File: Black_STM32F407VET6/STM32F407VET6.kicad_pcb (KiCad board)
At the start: 2 copper layers, 97 parts, among them J1 T0, J10 - HotBed +, J11 Heater0, J12 X-, J13 Y-, J14 Z-, J15 Z+, J16 USB_B, J17 X_logic, J18 Y_logic, J19 Z_logic, J2 T1, J20 E0_logic, J22 Left, J23 EXP2, J24 LCD2004, J25 Bottom, J26 Right, J27 Z_motor, J28 LIGHTS, J29 Z, J3 TB, J30 Z, J33 X_motor, J34 Y_motor, J36 E0_motor, J38 X, J39 Y, J4 TC, J41 E0, J43 Heater1, J44 COM, J47 I2C, J48 SPI, J49 SPI, J5 + VIN -, J50 SDIO, J51 Servo, J52 Servo, J53 PowerSelect, J54 Power, J55 PD11, J56 Power, J6 Fan3, J7 Fan2, J8 Fan1, J9 Fan0, Q1 BCX70, Q10 BCX70, Q11 BCX70, Q12 IRLR8726PBF, Q13 IRLR8726PBF, Q14 IRLR8726PBF, Q2 BCX70, Q3 BCX70, Q4 IRLML0030TRPBF, Q5 BCX70, Q6 IRLML0030TRPBF, Q7 IRLML0030TRPBF, Q8 IRLML0030TRPBF, Q9 BCX70, SW1 Boot0, U5 AT24CS01-SSHM

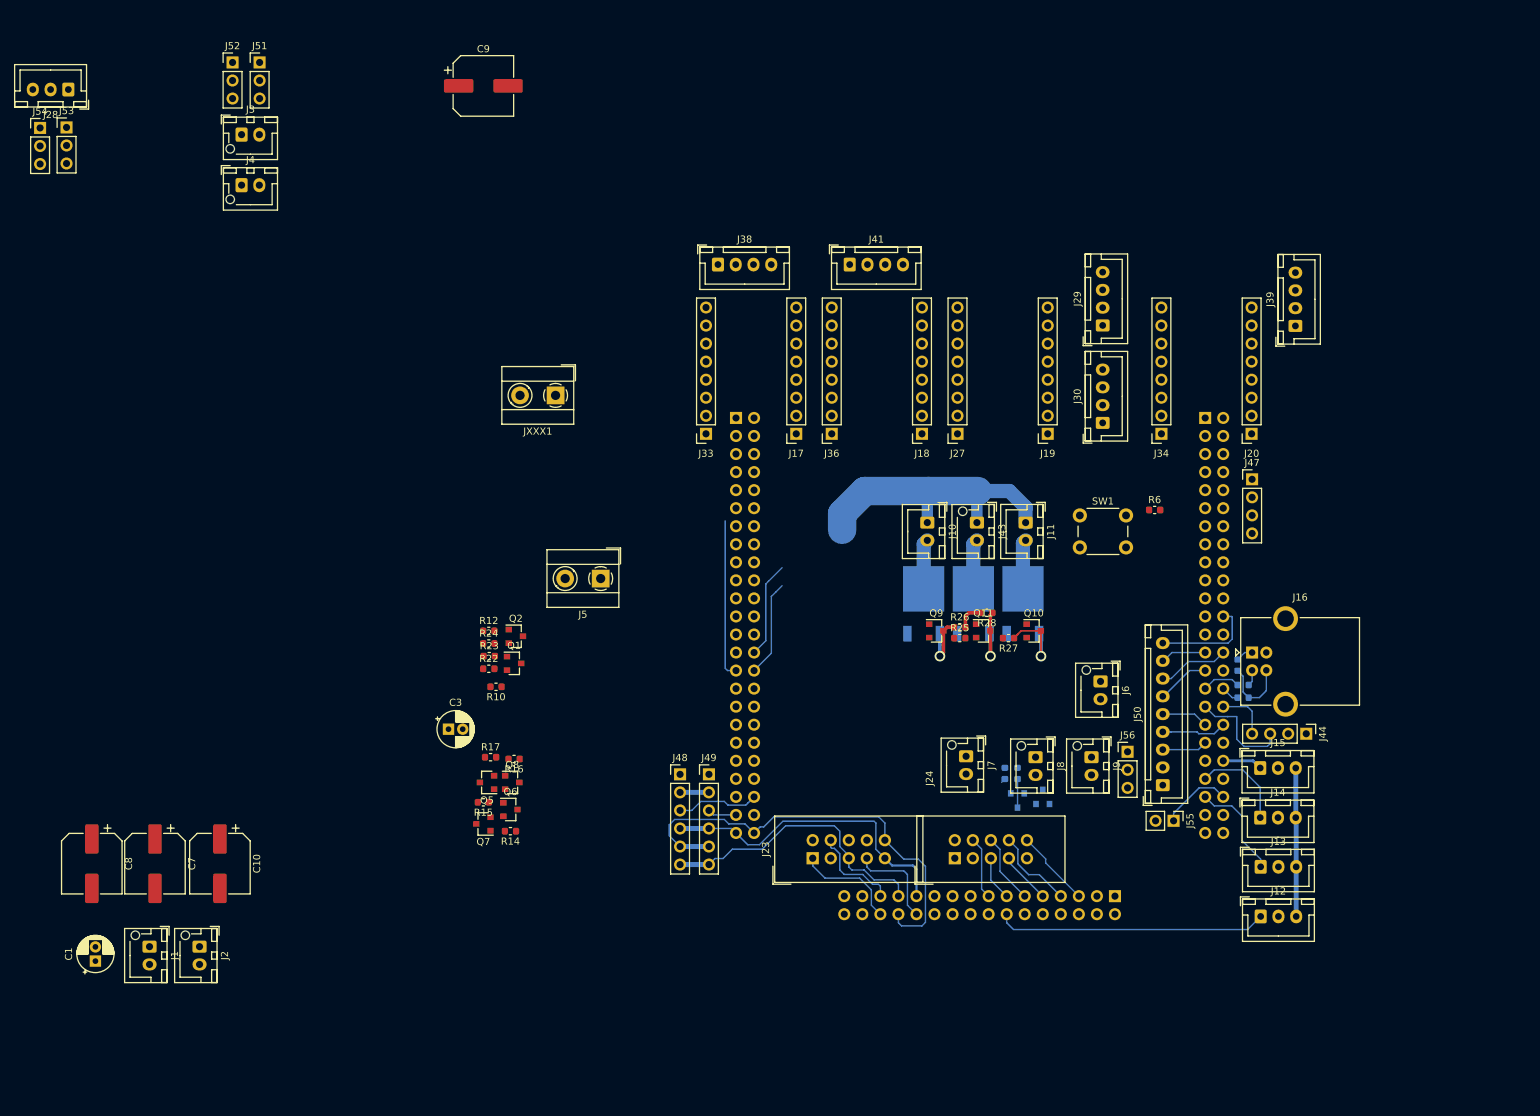
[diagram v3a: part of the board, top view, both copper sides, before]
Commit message: Rework of the PCB, made footprint for the motor drivers.
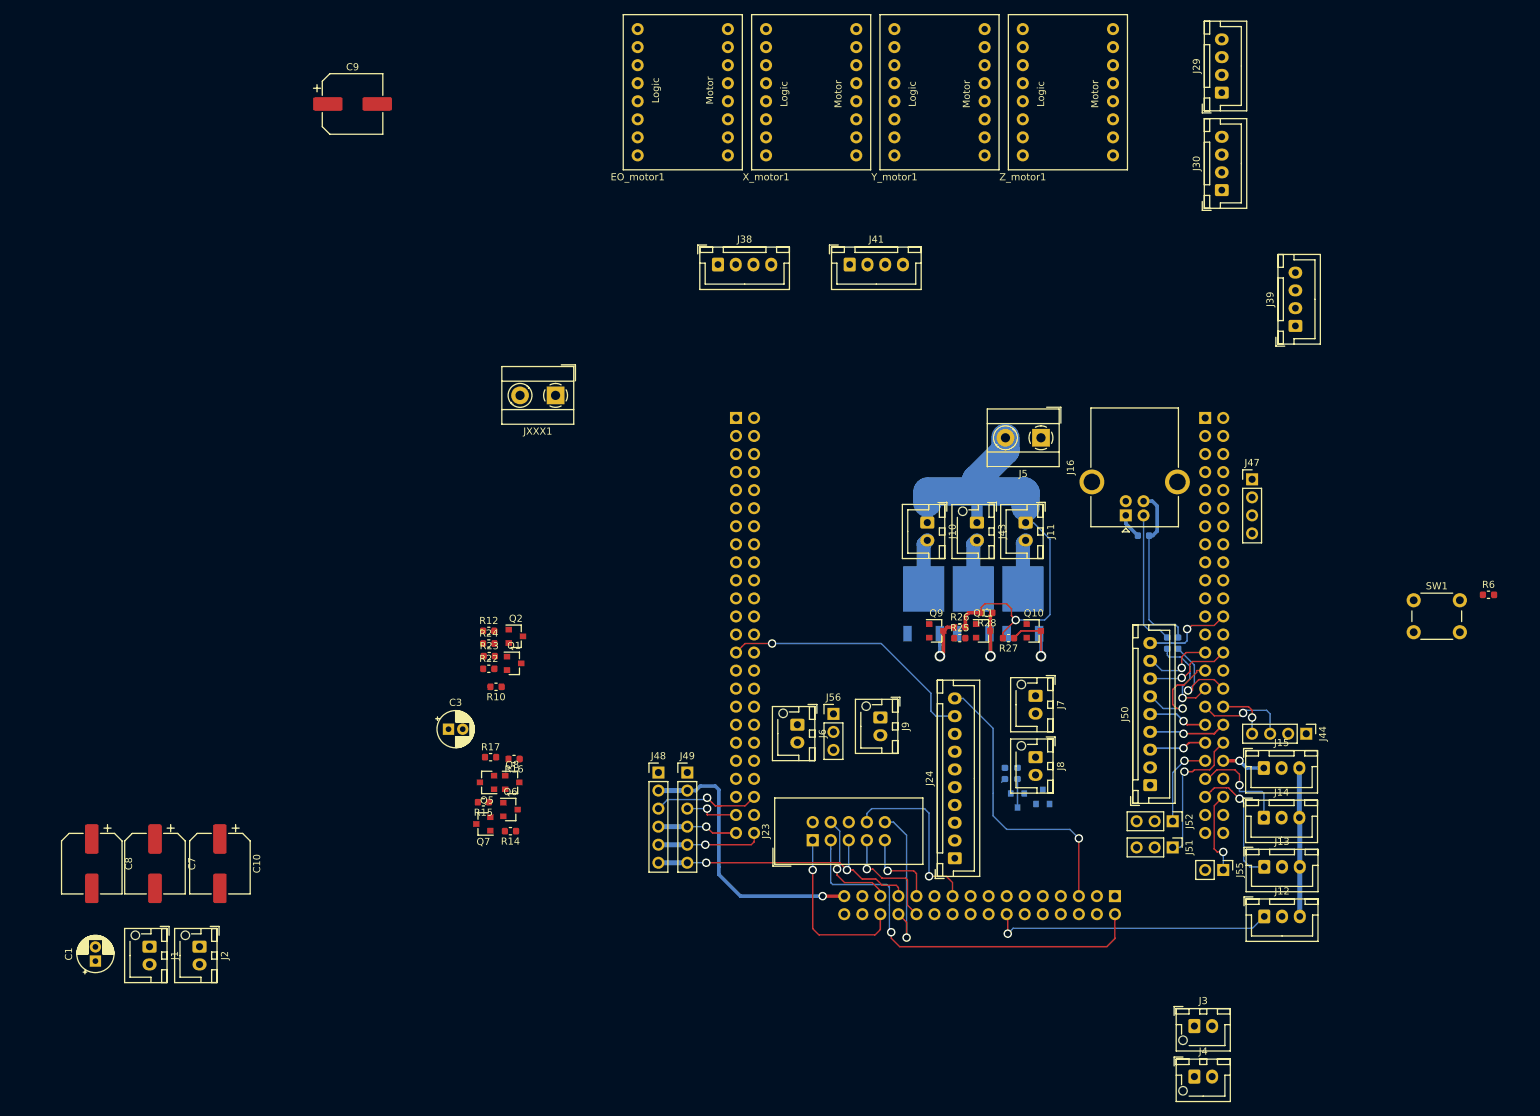
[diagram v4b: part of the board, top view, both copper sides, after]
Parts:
- removed J17: X_logic, Connector_PinSocket_2.54mm:PinSocket_1x08_P2.54mm_Vertical
- removed J18: Y_logic, Connector_PinSocket_2.54mm:PinSocket_1x08_P2.54mm_Vertical
- removed J19: Z_logic, Connector_PinSocket_2.54mm:PinSocket_1x08_P2.54mm_Vertical
- removed J20: E0_logic, Connector_PinSocket_2.54mm:PinSocket_1x08_P2.54mm_Vertical
- removed J27: Z_motor, Connector_PinSocket_2.54mm:PinSocket_1x08_P2.54mm_Vertical
- removed J28: LIGHTS, Connector_JST:JST_XH_B3B-XH-A_1x03_P2.50mm_Vertical
- removed J33: X_motor, Connector_PinSocket_2.54mm:PinSocket_1x08_P2.54mm_Vertical
- removed J34: Y_motor, Connector_PinSocket_2.54mm:PinSocket_1x08_P2.54mm_Vertical
- removed J36: E0_motor, Connector_PinSocket_2.54mm:PinSocket_1x08_P2.54mm_Vertical
- removed J53: PowerSelect, Connector_PinHeader_2.54mm:PinHeader_1x03_P2.54mm_Vertical
- removed J54: Power, Connector_PinHeader_2.54mm:PinHeader_1x03_P2.54mm_Vertical
- added EO_motor1: Step_stick, Motor_driver:Motor, F.Cu at (106.0, 48.9)
- added X_motor1: Step_stick, Motor_driver:Motor, F.Cu at (124.1, 48.9)
- added Y_motor1: Step_stick, Motor_driver:Motor, F.Cu at (142.2, 48.9)
- added Z_motor1: Step_stick, Motor_driver:Motor, F.Cu at (160.3, 48.9)
- C10, C7, C8, C9: value 100uF 35V -> 100uF
- J24: footprint Connector_IDC:IDC-Header_2x05_P2.54mm_Vertical -> Connector_JST:JST_XH_B10B-XH-A_1x10_P2.50mm_Vertical
- moved J3 183.7 mm to (186.4, 169.4)
- moved J4 183.7 mm to (186.4, 176.5)
- moved J52 170.1 mm to (183.4, 140.6), turned to 270 degrees
- moved J51 169.5 mm to (183.4, 144.3), turned to 270 degrees
- moved J5 65.1 mm to (164.8, 86.6)
- moved R6 48.5 mm to (227.8, 108.7)
- moved SW1 48.5 mm to (217.3, 109.5)
- moved J6 43.1 mm to (130.6, 127.0)
- moved J56 41.7 mm to (135.6, 125.5)
- moved J29 36.8 mm to (190.3, 38.0)
- moved J30 36.8 mm to (190.3, 51.7)
- moved J9 30.2 mm to (142.2, 126.0)
- moved J16 26.2 mm to (176.8, 97.5), turned to 90 degrees
- moved R5 22.5 mm to (179.3, 100.4), turned to 180 degrees
- moved C9 18.6 mm to (67.9, 39.6)
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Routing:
- net Reset: track 0.00 -> 57.7 mm, vias 0 -> 1
- net KEYPAD_PIN: track 0.00 -> 37.0 mm, vias 0 -> 1
- net 3V3: track 4.06 -> 39.8 mm, vias 0 -> 1
- net LCD7: track 10.9 -> 41.0 mm, vias 0 -> 1
- net MISO: track 63.5 -> 36.9 mm, vias 0 -> 2
- net 12V: track 45.5 -> 71.1 mm, vias 0 -> 1
- net EN1: track 0.00 -> 25.0 mm, vias 0 -> 1
- net Tmc_MISO: track 22.4 -> 0.00 mm
- net CLK: track 44.3 -> 23.2 mm, vias 0 -> 2
- net PWM2: track 0.00 -> 20.2 mm, vias 0 -> 1
- net Net-(J16-Pad2): track 2.27 -> 19.5 mm
- net Net-(J16-Pad3): track 10.2 -> 25.0 mm
- net Tmc_MOSI: track 13.6 -> 0.00 mm
- net Tmc_SCK: track 13.6 -> 0.00 mm
- net PWM1: track 0.00 -> 12.1 mm, vias 0 -> 1
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
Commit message: Power connectors - Removed left side holes to make room for Heater and Bed traces - Moved spi connectors, temperature connectors, fan connectors - Assigned correct footprints to power connectors (KF7.62_2P) 	- Downloaded from: https://github.com/StefanHamminga/SH_Connectors.pretty
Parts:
- removed J22: Left, Connector_PinSocket_2.54mm:PinSocket_2x24_P2.54mm_Vertical
- added J17: Left Analog, Connector_PinHeader_2.54mm:PinHeader_2x11_P2.54mm_Vertical, F.Cu at (121.9, 96.5)
- added J18: Left Spi, Connector_PinHeader_2.54mm:PinHeader_2x03_P2.54mm_Vertical, F.Cu at (121.9, 137.2)
- added J28: LIGHTS, Connector_JST:JST_XH_B3B-XH-A_1x03_P2.50mm_Vertical, F.Cu at (184.5, 154.1)
- added J53: PowerSelect, Connector_PinHeader_2.54mm:PinHeader_1x03_P2.54mm_Vertical, F.Cu at (153.7, 117.1)
- added J54: Power, Connector_PinHeader_2.54mm:PinHeader_1x03_P2.54mm_Vertical, F.Cu at (153.5, 127.5)
- J10: footprint Connector_JST:JST_XH_B2B-XH-A_1x02_P2.50mm_Vertical -> SH_Connectors:KF7.62_2P
- J11: footprint Connector_JST:JST_XH_B2B-XH-A_1x02_P2.50mm_Vertical -> TerminalBlock:TerminalBlock_bornier-2_P5.08mm
- J24: footprint Connector_JST:JST_XH_B10B-XH-A_1x10_P2.50mm_Vertical -> Connector_IDC:IDC-Header_2x05_P2.54mm_Vertical
- J43: footprint Connector_JST:JST_XH_B2B-XH-AM_1x02_P2.50mm_Vertical -> TerminalBlock:TerminalBlock_bornier-2_P5.08mm
- J5: footprint TerminalBlock_MetzConnect:TerminalBlock_MetzConnect_Type055_RT01502HDWU_1x02_P5.00mm_Horizontal -> SH_Connectors:KF7.62_2P
- JXXX1: footprint TerminalBlock_MetzConnect:TerminalBlock_MetzConnect_Type055_RT01502HDWU_1x02_P5.00mm_Horizontal -> TerminalBlock:TerminalBlock_bornier-2_P5.08mm
- R6: moved to B.Cu
- moved J4 110.3 mm to (131.4, 80.9), turned to 270 degrees
- moved J1 105.1 mm to (131.1, 107.0)
- moved J2 104.0 mm to (131.3, 98.1)
- moved J3 97.1 mm to (131.4, 89.4), turned to 270 degrees
- moved U5 96.2 mm to (182.2, 97.6), turned to 180 degrees
- moved Q10 89.6 mm to (77.4, 90.4)
- moved Q13 89.6 mm to (75.8, 86.6)
- moved Q12 89.6 mm to (61.9, 86.6)
- moved Q14 89.6 mm to (68.9, 86.6)
- moved Q9 89.6 mm to (63.7, 90.4)
- moved R27 89.6 mm to (73.8, 91.4)
- moved Q11 89.6 mm to (70.3, 90.4)
- moved R25 89.6 mm to (67.0, 91.4)
- moved R26 89.6 mm to (67.0, 89.9)
- moved R28 89.6 mm to (70.8, 87.8)
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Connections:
- EO_motor1 pad 1: E0_Dir -> E0_En
- EO_motor1 pad 2: E0_Step -> Tmc_MOSI
- EO_motor1 pad 3: Net-(EO_motor1-Pad3) -> Tmc_SCK
- EO_motor1 pad 4: Tmc_MISO -> E0_CS
- EO_motor1 pad 5: E0_CS -> Tmc_MISO
- EO_motor1 pad 6: Tmc_SCK -> Net-(EO_motor1-Pad6)
- EO_motor1 pad 7: Tmc_MOSI -> E0_Step
- EO_motor1 pad 8: E0_En -> E0_Dir
- J26 pad 6: Net-(J26-Pad6) -> GND
- X_motor1 pad 1: X_Dir -> X_En
- X_motor1 pad 2: X_Step -> Tmc_MOSI
- X_motor1 pad 3: Net-(X_motor1-Pad3) -> Tmc_SCK
- X_motor1 pad 4: Tmc_MISO -> X_CS
- X_motor1 pad 5: X_CS -> Tmc_MISO
- X_motor1 pad 6: Tmc_SCK -> Net-(X_motor1-Pad6)
- X_motor1 pad 7: Tmc_MOSI -> X_Step
- X_motor1 pad 8: X_En -> X_Dir
- Y_motor1 pad 1: Y_Dir -> Y_En
- Y_motor1 pad 2: Y_CS -> Tmc_MOSI
- Y_motor1 pad 3: Net-(Y_motor1-Pad3) -> Tmc_SCK
- Y_motor1 pad 4: Tmc_MISO -> Y_CS
- Y_motor1 pad 5: Y_Step -> Tmc_MISO
- Y_motor1 pad 6: Tmc_SCK -> Net-(Y_motor1-Pad6)
- Y_motor1 pad 7: Tmc_MOSI -> Y_Step
- Y_motor1 pad 8: Y_En -> Y_Dir
- Z_motor1 pad 1: Z_Dir -> Z_En
- Z_motor1 pad 2: Z_Step -> Tmc_MOSI
- Z_motor1 pad 3: Net-(Z_motor1-Pad3) -> Tmc_SCK
- Z_motor1 pad 4: Tmc_MISO -> Z_CS
- Z_motor1 pad 5: Z_CS -> Tmc_MISO
- Z_motor1 pad 6: Tmc_SCK -> Net-(Z_motor1-Pad6)
- Z_motor1 pad 7: Tmc_MOSI -> Z_Step
- Z_motor1 pad 8: Z_En -> Z_Dir
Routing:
- net GND: track 0.00 -> 108.8 mm
- net Net-(J43-Pad2): track 7.04 -> 69.7 mm
- net Net-(J11-Pad2): track 6.99 -> 55.3 mm
- net 12V: track 71.1 -> 119.1 mm
- net KEYPAD_PIN: track 37.0 -> 68.0 mm
- net LCD7: track 41.0 -> 12.6 mm
- net Net-(J10-Pad2): track 7.04 -> 33.7 mm
- net 3V3: track 39.8 -> 65.1 mm, vias 1 -> 2
- net Net-(J26-Pad5): track 0.00 -> 20.9 mm, vias 0 -> 1
- net SCL: track 0.00 -> 20.4 mm, vias 0 -> 1
- net CLK: track 23.2 -> 42.9 mm
- net SDA: track 0.00 -> 16.8 mm, vias 0 -> 1
- net Net-(J16-Pad3): track 25.0 -> 9.47 mm
- net LCD6: track 0.80 -> 13.4 mm, vias 0 -> 1
- net LCD5: track 0.00 -> 11.6 mm, vias 0 -> 1
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
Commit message: Left side  - Temperature sensors  - Capacitor package change  - Reworked left side symbols
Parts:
- removed J18: Left Spi, Connector_PinHeader_2.54mm:PinHeader_2x03_P2.54mm_Vertical
- added U1: LeftAnalog, Connector_PinHeader_2.54mm:PinHeader_2x11_P2.54mm_Vertical, F.Cu at (121.9, 96.5)
- added U2: Left5V, Connector_PinHeader_2.54mm:PinHeader_2x02_P2.54mm_Vertical, F.Cu at (121.9, 86.4)
- C1, C2, C3, C4: value 10uF 16V -> 10uF 25V; footprint Capacitor_THT:CP_Radial_D5.0mm_P2.00mm -> Capacitor_THT:CP_Radial_D4.0mm_P2.00mm
- J17: value Left Analog -> LeftSpi; footprint Connector_PinHeader_2.54mm:PinHeader_2x11_P2.54mm_Vertical -> Connector_PinHeader_2.54mm:PinHeader_2x03_P2.54mm_Vertical
- moved R1 151.4 mm to (127.3, 111.3), turned to 270 degrees
- moved R2 150.2 mm to (127.3, 107.2), turned to 90 degrees
- moved R4 145.2 mm to (127.3, 85.1), turned to 90 degrees
- moved R3 143.4 mm to (127.3, 90.3), turned to 270 degrees
- moved C2 139.7 mm to (137.5, 100.7), turned to 90 degrees
- moved C4 126.3 mm to (137.5, 83.2), turned to 90 degrees
- moved C1 117.6 mm to (137.8, 109.4)
- moved C3 66.4 mm to (137.5, 92.0), turned to 90 degrees
- moved EO_motor1 40.9 mm to (176.8, 82.0)
- moved J17 40.6 mm to (121.9, 137.2)
- moved Q5 23.9 mm to (87.9, 159.0)
- moved Q7 23.1 mm to (101.1, 160.0)
- moved Y_motor1 22.1 mm to (142.1, 81.9)
- moved Z_motor1 21.8 mm to (159.5, 82.0)
- moved R21 13.7 mm to (276.8, 36.4)
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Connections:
- J17 pad 1: X_Step -> Net-(J17-Pad1)
- J17 pad 2: Y_CS -> SS1
- J17 pad 3: X_CS -> SS2
- J17 pad 4: Y_Step -> Net-(J17-Pad4)
- J17 pad 5: X_En -> CLK
- J17 pad 6: Y_Dir -> MISO
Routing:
- net TC: track 0.00 -> 38.3 mm, vias 0 -> 1
- net TB: track 0.00 -> 26.3 mm, vias 0 -> 1
- net KEYPAD_PIN: track 68.0 -> 42.2 mm, vias 1 -> 0
- net T0: track 0.00 -> 17.6 mm, vias 0 -> 1
- net 3V3: track 65.1 -> 81.9 mm, vias 2 -> 4
- net T1: track 0.00 -> 11.7 mm, vias 0 -> 1
- net MOSI: track 34.2 -> 45.8 mm
- net SS1: track 10.7 -> 22.0 mm
- net CLK: track 42.9 -> 47.2 mm
- net SS2: track 17.7 -> 13.4 mm
- net MISO: track 46.8 -> 43.8 mm
